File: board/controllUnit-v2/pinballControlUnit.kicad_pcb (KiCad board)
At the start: 2 copper layers, 66 x 48.3 mm, 47 parts, among them J1 Conn_01x02_Male, J10 Screw_Terminal_01x02, J11 Screw_Terminal_01x02, J12 Screw_Terminal_01x02, J2 Conn_01x04_Male, J3 Conn_01x08_Male, J4 Conn_01x08_Male, J5 Conn_01x08_Male, J6 AudioJack2, J7 Conn_01x02_Male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

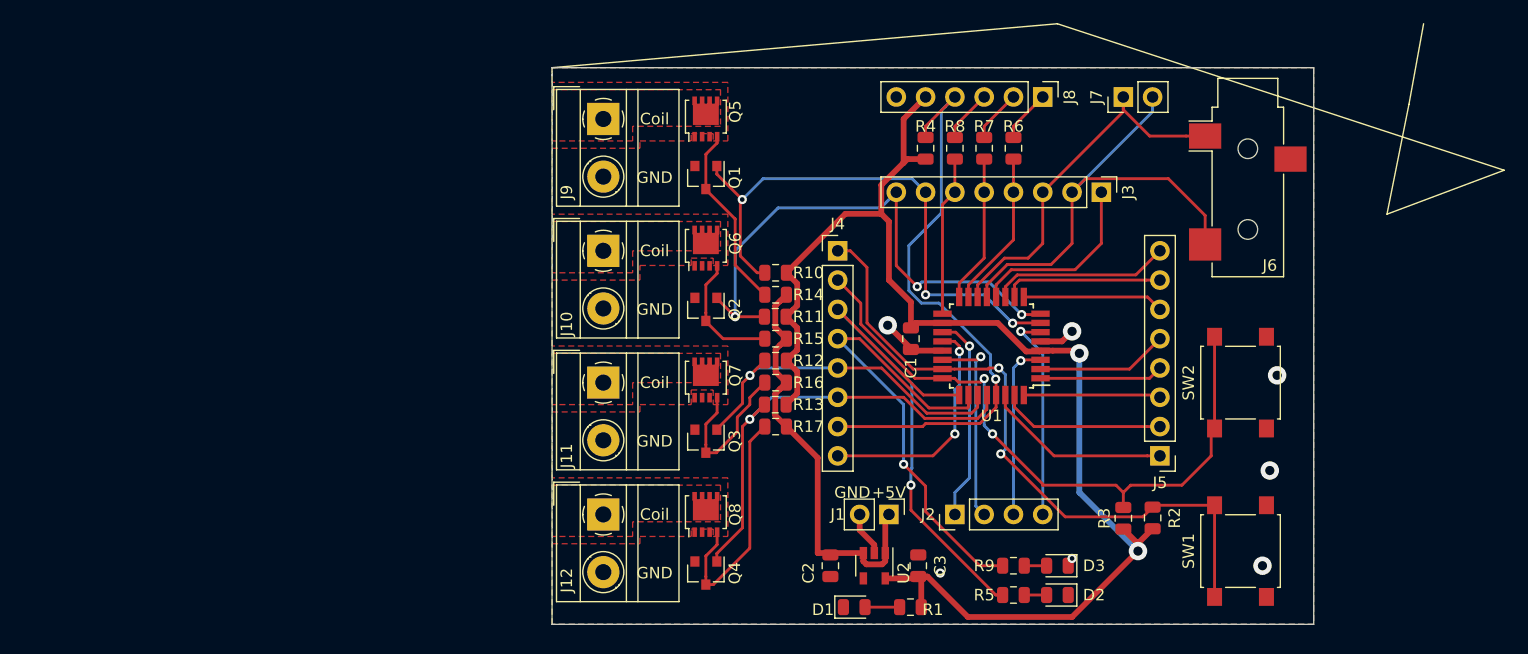
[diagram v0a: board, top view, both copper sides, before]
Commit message: Leiterplatte gelayoutet
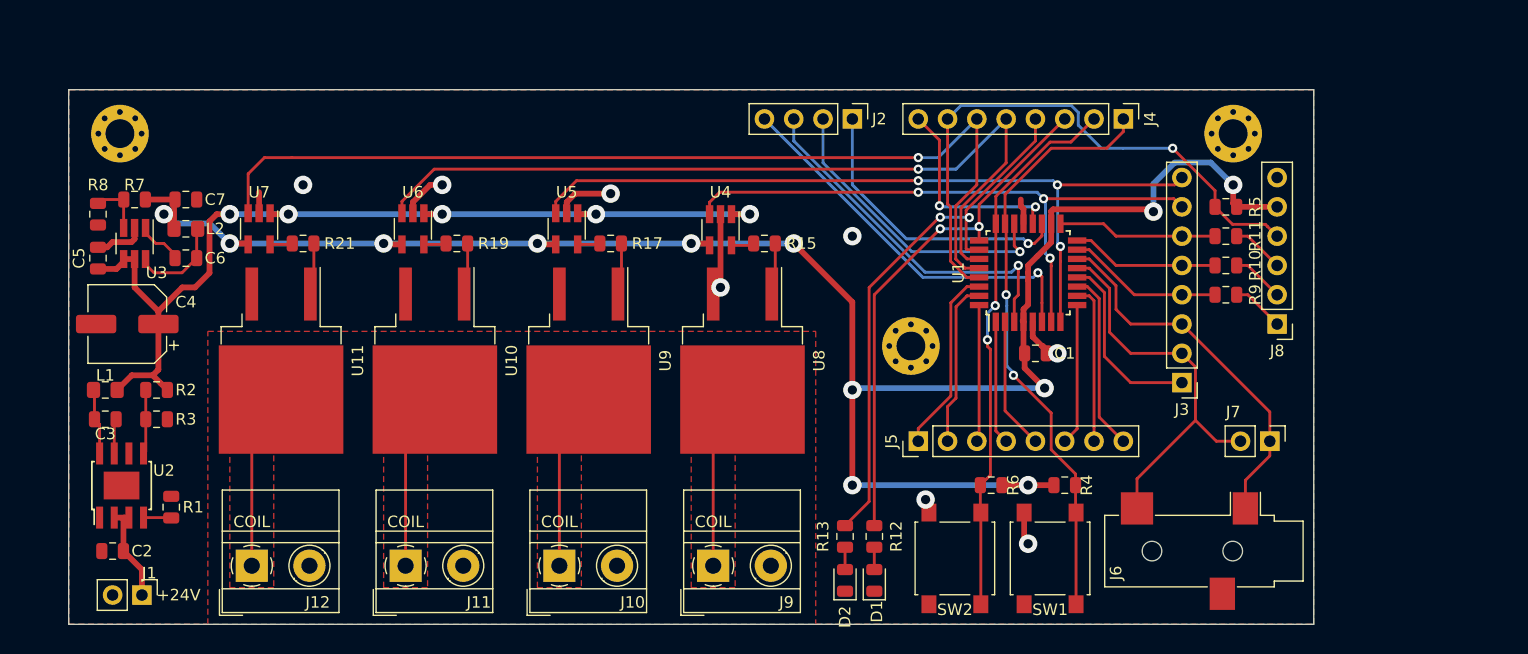
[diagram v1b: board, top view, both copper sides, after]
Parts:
- removed D3: LED, LED_SMD:LED_0805_2012Metric
- removed Q1, Q2, Q3, Q4: BSS138, Package_TO_SOT_SMD:SOT-23
- removed Q5, Q6, Q7, Q8: BUK9M85-60EX, Package_TO_SOT_SMD:LFPAK33
- removed R14, R16: 10k, Resistor_SMD:R_0805_2012Metric
- added C4: 47u, Capacitor_SMD:CP_Elec_6.3x3.9, F.Cu at (26.0, 84.5)
- added C5: 2.2u, Capacitor_SMD:C_0805_2012Metric, F.Cu at (23.5, 78.7)
- added C6: 0.1u, Capacitor_SMD:C_0805_2012Metric, F.Cu at (31.1, 78.7)
- added C7: 22u, Capacitor_SMD:C_0805_2012Metric, F.Cu at (31.1, 73.7)
- added L1: 68u, Inductor_SMD:L_0805_2012Metric_Pad1.15x1.40mm_HandSolder, F.Cu at (24.1, 90.2)
- added L2: 12u, Inductor_SMD:L_0805_2012Metric_Pad1.15x1.40mm_HandSolder, F.Cu at (31.1, 76.2)
- added R19: 100, Resistor_SMD:R_0805_2012Metric, F.Cu at (54.6, 77.5)
- added R21: 100, Resistor_SMD:R_0805_2012Metric, F.Cu at (41.3, 77.5)
- added REF**: MountingHole_2.5mm_Pad_Via, MountingHole:MountingHole_2.5mm_Pad_Via, F.Cu at (94.0, 86.4)
- added REF**: MountingHole_2.5mm_Pad_Via, MountingHole:MountingHole_2.5mm_Pad_Via, F.Cu at (121.9, 67.9)
- added REF**: MountingHole_2.5mm_Pad_Via, MountingHole:MountingHole_2.5mm_Pad_Via, F.Cu at (25.4, 67.9)
- added U10: STB16NF06L, Package_TO_SOT_SMD:TO-263-2, F.Cu at (52.7, 87.6)
- added U11: STB16NF06L, Package_TO_SOT_SMD:TO-263-2, F.Cu at (39.4, 87.6)
- added U3: TPS560430, Package_TO_SOT_SMD:SOT-23-6_Handsoldering, F.Cu at (26.7, 77.5)
- added U4: PM8841, Package_TO_SOT_SMD:SOT-23-5_HandSoldering, F.Cu at (77.5, 76.3)
- added U5: PM8841, Package_TO_SOT_SMD:SOT-23-5_HandSoldering, F.Cu at (64.1, 76.2)
- added U6: PM8841, Package_TO_SOT_SMD:SOT-23-5_HandSoldering, F.Cu at (50.8, 76.2)
- added U7: PM8841, Package_TO_SOT_SMD:SOT-23-5_HandSoldering, F.Cu at (37.5, 76.2)
- added U8: STB16NF06L, Package_TO_SOT_SMD:TO-263-2, F.Cu at (79.4, 87.6)
- added U9: STB16NF06L, Package_TO_SOT_SMD:TO-263-2, F.Cu at (66.0, 87.6)
- C2: value 1u -> 2.2u
- C3: value 1u -> 2.2n
- R1: value 100 -> 100k
- R10, R11: value 10k -> 1k
- R12, R13, R15, R17: value 10k -> 100
- R2: value 10k -> 448k
- R3: value 10k -> 49.9k
- R5: value 100 -> 10k
- R6: value 1k -> 10k
- R7: value 1k -> 51k
- R8: value 1k -> 22.1k
- R9: value 100 -> 1k
- U2: value MCP1802 -> LM5164; footprint Package_TO_SOT_SMD:SOT-23-5 -> Package_SO:TI_SO-PowerPAD-8
- moved R2 87.1 mm to (28.6, 90.2), turned to 180 degrees
- moved R3 84.3 mm to (28.6, 92.7), turned to 0 degrees
- moved R8 74.5 mm to (23.5, 74.9)
- moved R7 73.8 mm to (26.7, 73.7), turned to 180 degrees
- moved C3 71.6 mm to (24.1, 92.7), turned to 0 degrees
- moved U2 65.6 mm to (25.5, 98.5), turned to 90 degrees
- moved J1 65.1 mm to (27.3, 108.0)
- moved R1 64.7 mm to (29.8, 100.3), turned to 90 degrees
- moved C2 62.2 mm to (24.8, 104.1), turned to 180 degrees
- moved J9 39.9 mm to (76.8, 105.4), turned to 0 degrees
- moved R11 39.7 mm to (121.3, 76.8), turned to 180 degrees
- moved R10 39.0 mm to (121.3, 79.4), turned to 180 degrees
- moved R5 38.4 mm to (121.3, 74.3), turned to 180 degrees
- moved J2 35.4 mm to (88.9, 66.7), turned to 270 degrees
- moved J6 32.6 mm to (119.4, 104.1), turned to 270 degrees
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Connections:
- C2 pad 1: +5V -> +24V
- C3 pad 1: +3V3 -> Net-(C3-Pad1)
- C3 pad 2: GND -> Net-(C3-Pad2)
- J1 pad 1: +5V -> +24V
- R1 pad 1: +3V3 -> Net-(R1-Pad1)
- R1 pad 2: Net-(D1-Pad2) -> GND
- R10 pad 1: FET1 -> Net-(J8-Pad2)
- R10 pad 2: +3V3 -> MISO
- R11 pad 1: FET2 -> Net-(J8-Pad3)
- R11 pad 2: +3V3 -> SCK
- R12 pad 1: FET3 -> LED1
- R12 pad 2: +3V3 -> Net-(D1-Pad2)
- R13 pad 1: FET4 -> LED2
- R13 pad 2: +3V3 -> Net-(D2-Pad2)
- R15 pad 2: +5V -> Net-(R15-Pad2)
- R17 pad 2: +5V -> Net-(R17-Pad2)
- R2 pad 1: +3V3 -> +12V
- R2 pad 2: SW1 -> Net-(R2-Pad2)
- R3 pad 1: +3V3 -> Net-(R2-Pad2)
- R3 pad 2: SW2 -> GND
- R4 pad 2: RESET -> SW1
- R5 pad 1: LED1 -> +3V3
- R5 pad 2: Net-(D2-Pad2) -> RESET
- R6 pad 1: Net-(J8-Pad1) -> +3V3
- R6 pad 2: MOSI -> SW2
- R7 pad 1: Net-(J8-Pad2) -> +3V3
- R7 pad 2: MISO -> Net-(R7-Pad2)
- R8 pad 1: Net-(J8-Pad3) -> Net-(R7-Pad2)
- R8 pad 2: SCK -> GND
- R9 pad 1: LED2 -> Net-(J8-Pad1)
- R9 pad 2: Net-(D3-Pad2) -> MOSI
- U2 pad 1: +5V -> GND
- U2 pad 2: GND -> +24V
- U2 pad 3: +5V -> +24V
- U2 pad 4: (no net) -> Net-(R1-Pad1)
- U2 pad 5: +3V3 -> Net-(R2-Pad2)
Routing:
- net +12V: track 0.00 -> 84.1 mm, vias 0 -> 5
- net +3V3: track 117.5 -> 171.3 mm, vias 2 -> 12
- net FET4: track 39.0 -> 83.8 mm
- net FET3: track 30.6 -> 71.4 mm
- net +5V: track 36.9 -> 0.00 mm
- net FET2: track 47.6 -> 68.6 mm
- net GND: track 12.7 -> 32.3 mm, vias 7 -> 8
- net Net-(R17-Pad1): track 21.1 -> 4.51 mm
- net Net-(Q1-Pad3): track 16.2 -> 0.00 mm
- net PA2: track 15.3 -> 31.4 mm
- net PA3: track 18.4 -> 34.0 mm
- net Net-(J9-Pad1): track 0.00 -> 15.5 mm
- net Net-(J10-Pad1): track 0.00 -> 15.5 mm
- net Net-(J12-Pad1): track 0.00 -> 15.5 mm
- net Net-(J11-Pad1): track 0.00 -> 15.5 mm
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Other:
- board size 66 x 48.3 mm -> 108 x 46.4 mm
- board text added: "+24V"
- board text added: "COIL"
- board text removed: "+5V"
- board text removed: "Coil"
- board text removed: "GND"

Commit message: Schaltregler Layout gemäss Datenblatt angepasst
TPS560430
LM5164
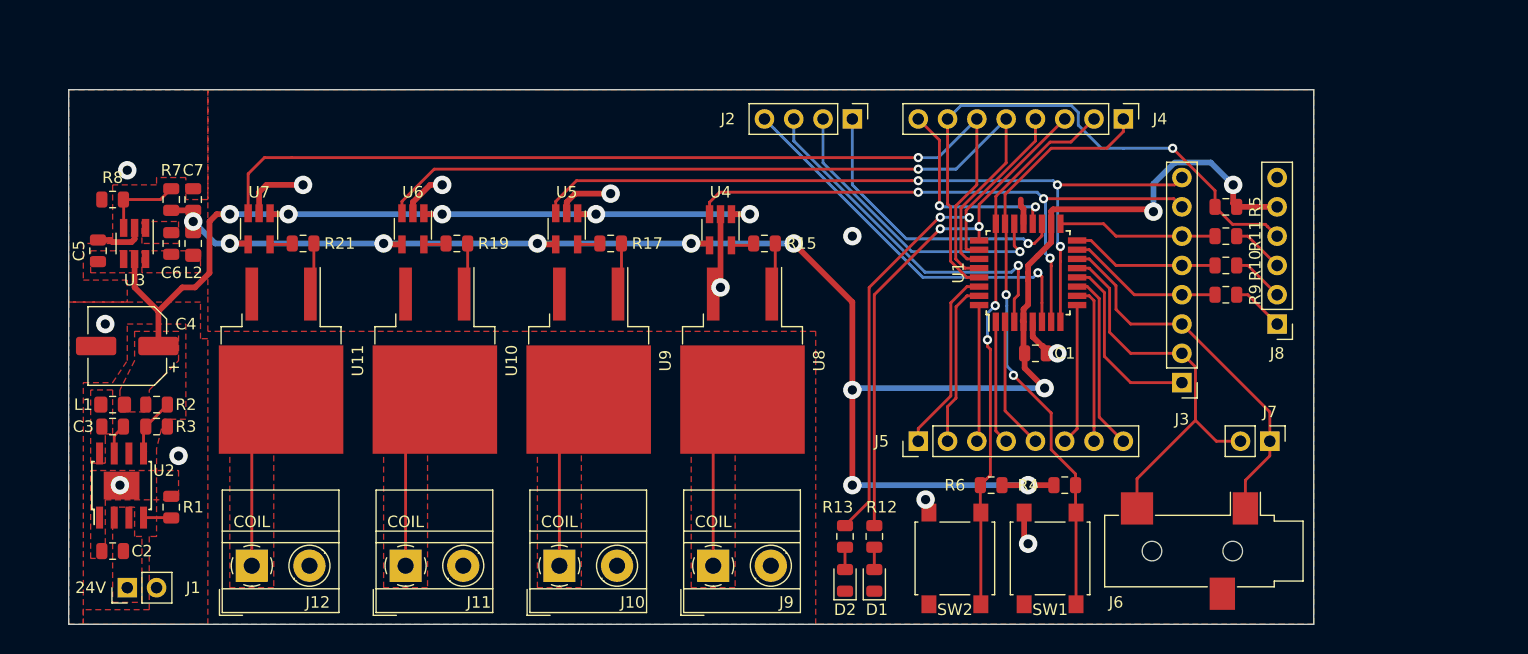
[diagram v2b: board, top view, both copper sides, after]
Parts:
- removed REF** (x3): MountingHole_2.5mm_Pad_Via, MountingHole:MountingHole_2.5mm_Pad_Via
- moved R7 3.17 mm to (29.8, 73.7), turned to 90 degrees
- moved C4 1.91 mm to (26.0, 86.4)
- moved R8 1.80 mm to (24.8, 73.7), turned to 180 degrees
- moved C6 1.80 mm to (29.8, 77.5), turned to 270 degrees
- moved J1 1.42 mm to (26.0, 107.3), turned to 90 degrees
- moved L1 1.42 mm to (24.8, 91.4)
- moved L2 1.42 mm to (31.8, 77.5), turned to 270 degrees
- moved R2 1.27 mm to (28.6, 91.4), turned to 0 degrees
- moved C3 0.90 mm to (24.8, 93.3)
- moved R3 0.64 mm to (28.6, 93.3)
- moved C7 0.64 mm to (31.8, 73.7), turned to 90 degrees
- moved C5 0.63 mm to (23.5, 78.1)
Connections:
- U2 pad 9: (no net) -> GND
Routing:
- net +12V: track 84.1 -> 72.2 mm
- net +24V: track 8.67 -> 0.00 mm
- net Net-(C6-Pad2): track 8.29 -> 0.46 mm
- net +3V3: track 171.3 -> 165.4 mm
- net Net-(C3-Pad1): track 5.73 -> 0.00 mm
- net Net-(C6-Pad1): track 4.09 -> 0.00 mm
- net GND: track 32.3 -> 36.3 mm, vias 8 -> 12
- net Net-(R7-Pad2): track 4.84 -> 7.00 mm
- added copper zone on F.Cu, net +12V
- added copper zone on F.Cu, net +24V
- added copper zone on F.Cu, net Net-(C3-Pad1)
- added copper zone on F.Cu, net Net-(C6-Pad1)
- added copper zone on F.Cu, net Net-(C6-Pad2)
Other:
- board text added: "24V"
- board text removed: "+24V"

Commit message: Schema+Layout fertig
Stückliste erstellt
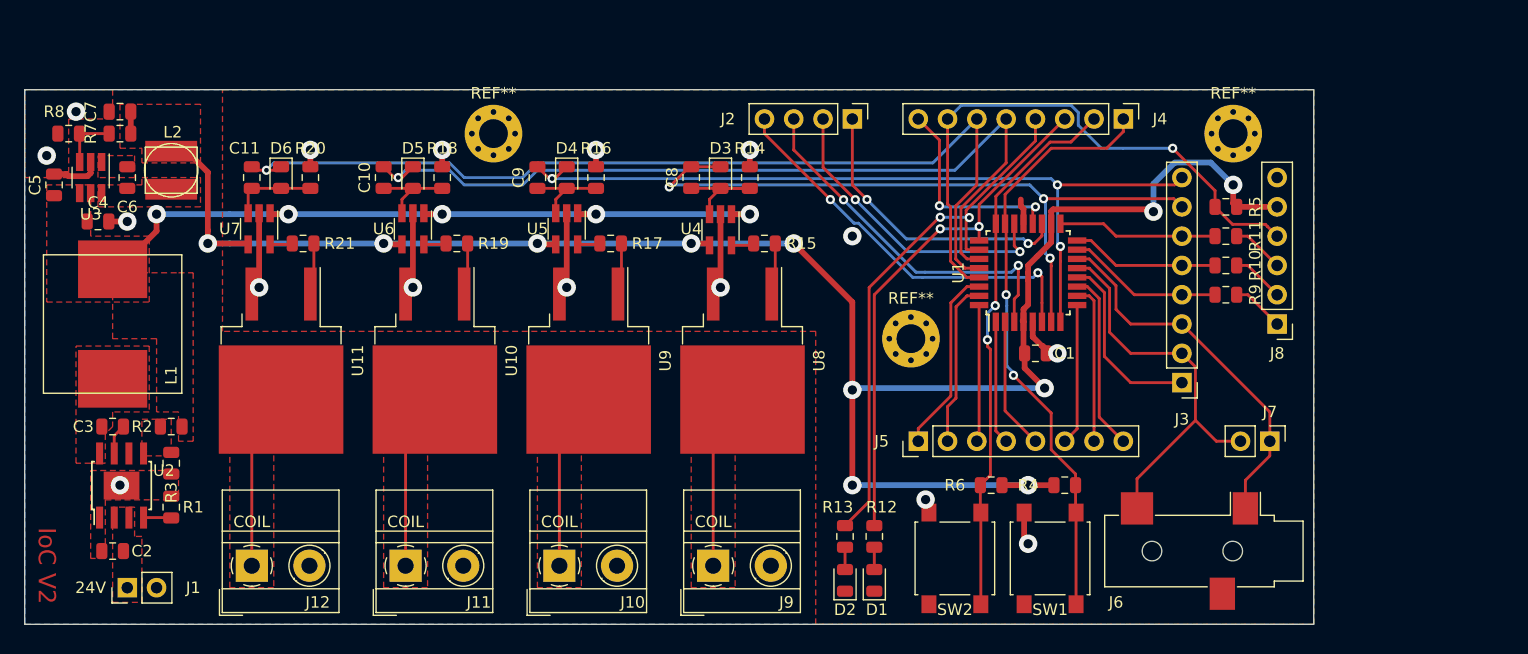
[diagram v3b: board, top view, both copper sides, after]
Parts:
- added C10: C, Capacitor_SMD:C_0805_2012Metric, F.Cu at (48.3, 71.8)
- added C11: C, Capacitor_SMD:C_0805_2012Metric, F.Cu at (36.8, 71.8)
- added C8: C, Capacitor_SMD:C_0805_2012Metric, F.Cu at (74.9, 71.8)
- added C9: C, Capacitor_SMD:C_0805_2012Metric, F.Cu at (61.6, 71.8)
- added D3: D, LED_SMD:LED_0805_2012Metric, F.Cu at (77.5, 71.8)
- added D4: D, LED_SMD:LED_0805_2012Metric, F.Cu at (64.1, 71.8)
- added D5: D, LED_SMD:LED_0805_2012Metric, F.Cu at (50.8, 71.8)
- added D6: D, LED_SMD:LED_0805_2012Metric, F.Cu at (39.4, 71.8)
- added R14: R, Resistor_SMD:R_0805_2012Metric, F.Cu at (80.0, 71.8)
- added R16: R, Resistor_SMD:R_0805_2012Metric, F.Cu at (66.7, 71.8)
- added R18: R, Resistor_SMD:R_0805_2012Metric, F.Cu at (53.3, 71.8)
- added R20: R, Resistor_SMD:R_0805_2012Metric, F.Cu at (41.9, 71.8)
- added REF**: MountingHole_2.5mm_Pad_Via, MountingHole:MountingHole_2.5mm_Pad_Via, F.Cu at (94.0, 85.7)
- added REF**: MountingHole_2.5mm_Pad_Via, MountingHole:MountingHole_2.5mm_Pad_Via, F.Cu at (57.8, 67.9)
- added REF**: MountingHole_2.5mm_Pad_Via, MountingHole:MountingHole_2.5mm_Pad_Via, F.Cu at (121.9, 67.9)
- C4: footprint Capacitor_SMD:CP_Elec_6.3x3.9 -> Capacitor_SMD:C_0805_2012Metric
- L1: footprint Inductor_SMD:L_0805_2012Metric_Pad1.15x1.40mm_HandSolder -> myFootPrints:L_MSS1246-683MLB
- L2: footprint Inductor_SMD:L_0805_2012Metric_Pad1.15x1.40mm_HandSolder -> myFootPrints:L_SDR0403-120ML
- moved C4 11.1 mm to (23.5, 75.6), turned to 0 degrees
- moved C7 9.92 mm to (25.4, 66.0), turned to 180 degrees
- moved R7 7.24 mm to (25.4, 67.9), turned to 180 degrees
- moved L1 6.98 mm to (24.8, 84.5), turned to 0 degrees
- moved C5 6.87 mm to (19.7, 72.4)
- moved R8 6.87 mm to (21.0, 67.9)
- moved U3 6.87 mm to (22.9, 71.8)
- moved C6 6.87 mm to (26.0, 71.8)
- moved L2 6.63 mm to (29.8, 71.1), turned to 0 degrees
- moved R3 3.42 mm to (29.8, 96.5), turned to 270 degrees
- moved R2 2.29 mm to (29.8, 93.3), turned to 180 degrees
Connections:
- U4 pad 3: FET1 -> Net-(C8-Pad1)
- U5 pad 3: FET2 -> Net-(C9-Pad1)
- U6 pad 3: FET3 -> Net-(C10-Pad1)
- U7 pad 3: FET4 -> Net-(C11-Pad1)
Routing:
- net GND: track 36.3 -> 47.9 mm, vias 12 -> 16
- net Net-(C8-Pad1): track 0.00 -> 10.3 mm
- net +3V3: track 165.4 -> 173.5 mm, vias 12 -> 11
- net +12V: track 72.2 -> 64.5 mm
- net Net-(C10-Pad1): track 0.00 -> 7.63 mm
- net Net-(C9-Pad1): track 0.00 -> 7.63 mm
- net FET1: track 54.1 -> 61.7 mm
- net Net-(C11-Pad1): track 0.00 -> 7.37 mm
- net Net-(R2-Pad2): track 5.37 -> 0.27 mm
- net FET3: track 71.4 -> 74.2 mm
- net FET2: track 68.6 -> 70.6 mm
- net Net-(R7-Pad2): track 7.00 -> 5.04 mm
- net FET4: track 83.8 -> 82.5 mm
- net PA3: track 34.0 -> 34.7 mm, vias 1 -> 2
- net PA2: track 31.4 -> 31.8 mm, vias 1 -> 2
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- added copper zone on F.Cu, net +3V3
- added copper zone on F.Cu, net Net-(R2-Pad2)
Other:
- board size 108 x 46.4 mm -> 111.8 x 46.4 mm
- board text added: "IoC V2"

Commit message: Leiterplatte soweit fertig
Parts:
- removed REF** (x3): MountingHole_2.5mm_Pad_Via, MountingHole:MountingHole_2.5mm_Pad_Via
- added C12: 100n, Capacitor_SMD:C_0805_2012Metric, F.Cu at (29.2, 76.8)
- added C13: 470n, Capacitor_SMD:C_0805_2012Metric, F.Cu at (78.7, 72.4)
- added C14: 470n, Capacitor_SMD:C_0805_2012Metric, F.Cu at (54.0, 75.2)
- added C15: 470n, Capacitor_SMD:C_0805_2012Metric, F.Cu at (67.3, 75.2)
- added C16: 470n, Capacitor_SMD:C_0805_2012Metric, F.Cu at (40.6, 75.2)
- added D10: D, LED_SMD:LED_0805_2012Metric, F.Cu at (45.1, 73.7)
- added D7: D, LED_SMD:LED_0805_2012Metric, F.Cu at (83.8, 73.7)
- added D8: D, LED_SMD:LED_0805_2012Metric, F.Cu at (71.8, 73.7)
- added D9: D, LED_SMD:LED_0805_2012Metric, F.Cu at (58.4, 73.7)
- added R22: R, Resistor_SMD:R_0805_2012Metric, F.Cu at (32.4, 73.7)
- added R23: 10, Resistor_SMD:R_0805_2012Metric, F.Cu at (85.1, 76.8)
- added R24: 10, Resistor_SMD:R_0805_2012Metric, F.Cu at (73.0, 76.8)
- added R25: 10, Resistor_SMD:R_0805_2012Metric, F.Cu at (59.7, 76.8)
- added R26: 100, Resistor_SMD:R_0805_2012Metric, F.Cu at (46.4, 76.8)
- added U12: LM4040DBZ-2.5, Package_TO_SOT_SMD:SOT-23, F.Cu at (32.4, 76.8)
- C2: footprint Capacitor_SMD:C_0805_2012Metric -> Capacitor_SMD:C_1206_3216Metric
- C4: footprint Capacitor_SMD:C_0805_2012Metric -> Capacitor_SMD:C_Elec_6.3x5.8
- R15, R17, R19: value 100 -> 50
- moved J1 5.75 mm to (20.3, 108.0), turned to 180 degrees
- moved C7 4.58 mm to (29.2, 63.5), turned to 0 degrees
- moved C5 4.45 mm to (19.7, 67.9)
- moved C6 4.44 mm to (26.0, 67.3)
- moved R7 4.44 mm to (25.4, 63.5)
- moved R8 4.44 mm to (21.0, 63.5)
- moved U3 4.44 mm to (22.9, 67.3)
- moved L2 3.81 mm to (29.8, 67.3)
- moved R17 2.62 mm to (70.5, 76.8), turned to 90 degrees
- moved R19 2.62 mm to (57.1, 76.8), turned to 90 degrees
- moved R21 2.62 mm to (43.8, 76.8), turned to 90 degrees
- moved C8 2.62 mm to (74.3, 69.2)
- moved D3 2.62 mm to (76.8, 69.2)
- moved C2 1.91 mm to (24.8, 106.0)
- moved C3 1.91 mm to (24.8, 95.2)
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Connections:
- U4 pad 4: +3V3 -> +2V5
- U5 pad 4: +3V3 -> +2V5
- U6 pad 4: +3V3 -> +2V5
- U7 pad 4: +3V3 -> +2V5
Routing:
- net +2V5: track 0.00 -> 57.0 mm, vias 0 -> 4
- net +3V3: track 173.5 -> 135.0 mm, vias 11 -> 6
- net +12V: track 64.5 -> 73.1 mm
- net GND: track 47.9 -> 55.0 mm, vias 16 -> 20
- net Net-(D8-Pad1): track 1.96 -> 8.46 mm
- net Net-(D9-Pad1): track 1.96 -> 8.46 mm
- net Net-(D10-Pad1): track 1.96 -> 8.46 mm
- net Net-(D7-Pad1): track 1.99 -> 7.22 mm
- net Net-(R17-Pad1): track 4.51 -> 8.39 mm
- net Net-(R19-Pad1): track 4.51 -> 8.39 mm
- net Net-(R21-Pad1): track 4.51 -> 7.96 mm
- net Net-(R15-Pad1): track 4.51 -> 7.31 mm
- net Net-(D8-Pad2): track 0.00 -> 2.38 mm
- net Net-(D7-Pad2): track 0.00 -> 2.38 mm
- net Net-(D9-Pad2): track 0.00 -> 2.38 mm
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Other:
- board size 111.8 x 46.4 mm -> 111.8 x 48.9 mm
- board text added: "+"
- board text removed: "24V"
